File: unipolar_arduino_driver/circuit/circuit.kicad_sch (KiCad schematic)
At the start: 4 parts, among them U1 ULN2803A

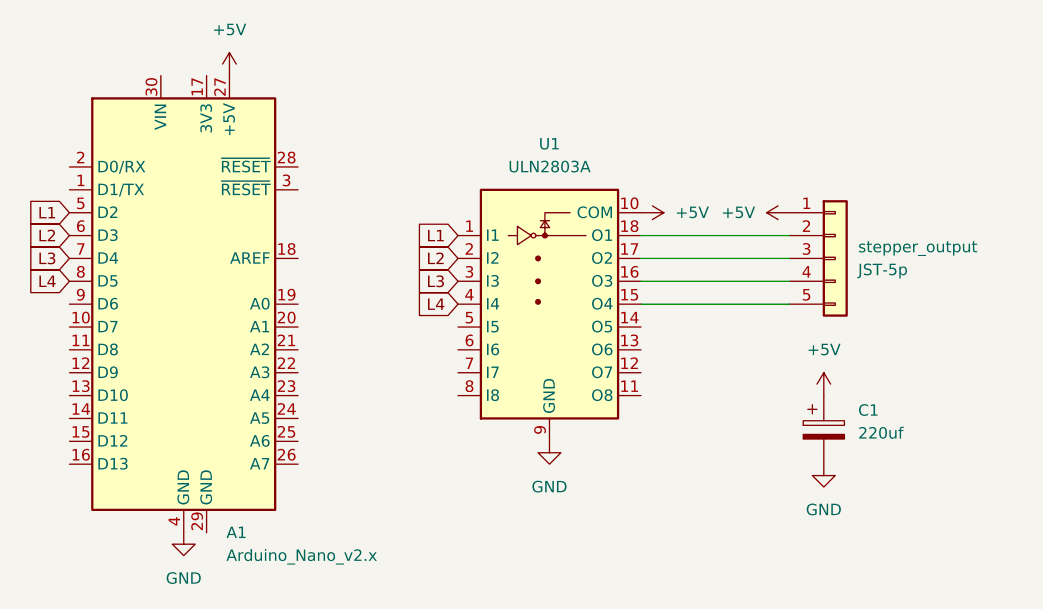
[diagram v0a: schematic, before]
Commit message: finished unipolar driver
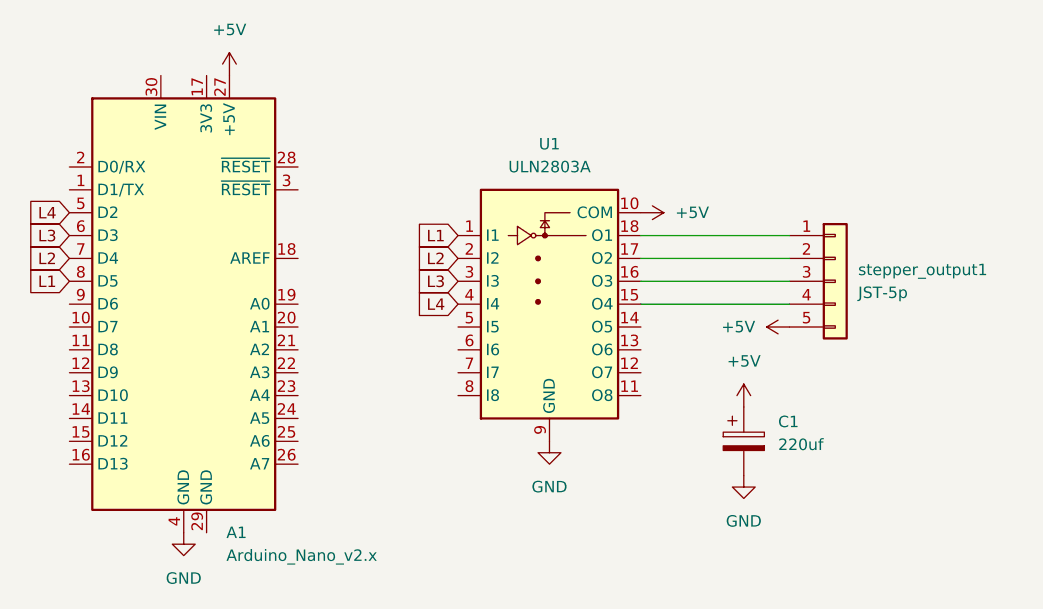
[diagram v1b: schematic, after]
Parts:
- renumbered stepper_output to stepper_output1
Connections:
- net +5V: now also stepper_output1.5 (Pin_5); no longer stepper_output1.1 (Pin_1)
- net L1: now also A1.8 (D5); no longer A1.5 (D2)
- net L2: now also A1.7 (D4); no longer A1.6 (D3)
- net L3: now also A1.6 (D3); no longer A1.7 (D4)
- net L4: now also A1.5 (D2); no longer A1.8 (D5)
- net at U1.18 (O1): now also stepper_output1.1 (Pin_1); no longer stepper_output1.2 (Pin_2)
- net at U1.17 (O2): now also stepper_output1.2 (Pin_2); no longer stepper_output1.3 (Pin_3)
- net at U1.16 (O3): now also stepper_output1.3 (Pin_3); no longer stepper_output1.4 (Pin_4)
- net at U1.15 (O4): now also stepper_output1.4 (Pin_4); no longer stepper_output1.5 (Pin_5)
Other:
- moved on the sheet: C1, stepper_output1
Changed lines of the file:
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@@
 	(global_label "L4"
 		(shape input)
-		(at 92.71 95.25 180)
+		(at 92.71 87.63 180)
 		(fields_autoplaced yes)
 		(effects
@@
 		)
 		(property "Intersheetrefs" "${INTERSHEET_REFS}"
-			(at 87.4872 95.25 0)
+			(at 87.4872 87.63 0)
 			(effects
 				(font
@@
 	(global_label "L3"
 		(shape input)
-		(at 92.71 92.71 180)
+		(at 92.71 90.17 180)
 		(fields_autoplaced yes)
 		(effects
@@
 		)
 		(property "Intersheetrefs" "${INTERSHEET_REFS}"
-			(at 87.4872 92.71 0)
+			(at 87.4872 90.17 0)
 			(effects
 				(font
@@
 	(global_label "L2"
 		(shape input)
-		(at 92.71 90.17 180)
+		(at 92.71 92.71 180)
 		(fields_autoplaced yes)
 		(effects
@@
 		)
 		(property "Intersheetrefs" "${INTERSHEET_REFS}"
-			(at 87.4872 90.17 0)
+			(at 87.4872 92.71 0)
 			(effects
 				(font
@@
 	(global_label "L1"
 		(shape input)
-		(at 92.71 87.63 180)
+		(at 92.71 95.25 180)
 		(fields_autoplaced yes)
 		(effects
@@
 		)
 		(property "Intersheetrefs" "${INTERSHEET_REFS}"
-			(at 87.4872 87.63 0)
+			(at 87.4872 95.25 0)
 			(effects
 				(font
@@
 	(symbol
 		(lib_id "Connector_Generic:Conn_01x05")
-		(at 177.8 92.71 0)
-		(unit 1)
-		(exclude_from_sim no)
-		(in_bom yes)
-		(on_board yes)
-		(dnp no)
-		(fields_autoplaced yes)
-		(property "Reference" "stepper_output"
-			(at 180.34 91.4399 0)
+		(at 177.8 95.25 0)
+		(unit 1)
+		(exclude_from_sim no)
+		(in_bom yes)
+		(on_board yes)
+		(dnp no)
+		(fields_autoplaced yes)
+		(property "Reference" "stepper_output1"
+			(at 180.34 93.9799 0)
 			(effects
 				(font
@@
 		)
 		(property "Value" "JST-5p"
-			(at 180.34 93.9799 0)
+			(at 180.34 96.5199 0)
 			(effects
 				(font
@@
 		)
 		(property "Footprint" "Connector_JST:JST_EH_B5B-EH-A_1x05_P2.50mm_Vertical"
-			(at 177.8 92.71 0)
+			(at 177.8 95.25 0)
 			(effects
 				(font
@@
 		)
 		(property "Datasheet" "~"
-			(at 177.8 92.71 0)
+			(at 177.8 95.25 0)
 			(effects
 				(font
@@
 		)
 		(property "Description" "Generic connector, single row, 01x05, script generated (kicad-library-utils/schlib/autogen/connector/)"
-			(at 177.8 92.71 0)
+			(at 177.8 95.25 0)
 			(effects
 				(font
@@
 			(project ""
 				(path "/d0bfccd7-cc06-4c1b-8a8c-9fcd948798c3"
-					(reference "stepper_output")
+					(reference "stepper_output1")
 					(unit 1)
 				)
@@
 	(symbol
 		(lib_id "power:+5V")
-		(at 172.72 87.63 90)
+		(at 172.72 100.33 90)
 		(unit 1)
 		(exclude_from_sim no)
@@
 		(fields_autoplaced yes)
 		(property "Reference" "#PWR04"
-			(at 176.53 87.63 0)
+			(at 176.53 100.33 0)
 			(effects
 				(font
@@
 		)
 		(property "Value" "+5V"
-			(at 168.91 87.6299 90)
+			(at 168.91 100.3299 90)
 			(effects
 				(font
@@
 		)
 		(property "Footprint" ""
-			(at 172.72 87.63 0)
+			(at 172.72 100.33 0)
 			(effects
 				(font
@@
 		)
 		(property "Datasheet" ""
-			(at 172.72 87.63 0)
+			(at 172.72 100.33 0)
 			(effects
 				(font
@@
 		)
 		(property "Description" "Power symbol creates a global label with name \"+5V\""
-			(at 172.72 87.63 0)
+			(at 172.72 100.33 0)
 			(effects
 				(font
@@
 	(symbol
 		(lib_id "power:GND")
-		(at 176.53 115.57 0)
+		(at 167.64 116.84 0)
 		(unit 1)
 		(exclude_from_sim no)
@@
 		(fields_autoplaced yes)
 		(property "Reference" "#PWR07"
-			(at 176.53 121.92 0)
+			(at 167.64 123.19 0)
 			(effects
 				(font
@@
 		)
 		(property "Value" "GND"
-			(at 176.53 120.65 0)
+			(at 167.64 121.92 0)
 			(effects
 				(font
@@
 		)
 		(property "Footprint" ""
-			(at 176.53 115.57 0)
+			(at 167.64 116.84 0)
 			(effects
 				(font
@@
 		)
 		(property "Datasheet" ""
-			(at 176.53 115.57 0)
+			(at 167.64 116.84 0)
 			(effects
 				(font
@@
 		)
 		(property "Description" "Power symbol creates a global label with name \"GND\" , ground"
-			(at 176.53 115.57 0)
+			(at 167.64 116.84 0)
 			(effects
 				(font
@@
 	(symbol
 		(lib_id "Device:C_Polarized")
-		(at 176.53 111.76 0)
+		(at 167.64 113.03 0)
 		(unit 1)
 		(exclude_from_sim no)
@@
 		(fields_autoplaced yes)
 		(property "Reference" "C1"
-			(at 180.34 109.6009 0)
+			(at 171.45 110.8709 0)
 			(effects
 				(font
@@
 		)
 		(property "Value" "220uf"
-			(at 180.34 112.1409 0)
+			(at 171.45 113.4109 0)
 			(effects
 				(font
@@
 		)
 		(property "Footprint" "Capacitor_THT:CP_Radial_D6.3mm_P2.50mm"
-			(at 177.4952 115.57 0)
+			(at 168.6052 116.84 0)
 			(effects
 				(font
@@
 		)
 		(property "Datasheet" "~"
-			(at 176.53 111.76 0)
+			(at 167.64 113.03 0)
 			(effects
 				(font
@@
 		)
 		(property "Description" "Polarized capacitor"
-			(at 176.53 111.76 0)
+			(at 167.64 113.03 0)
 			(effects
 				(font
@@
 	(symbol
 		(lib_id "power:+5V")
-		(at 176.53 107.95 0)
+		(at 167.64 109.22 0)
 		(unit 1)
 		(exclude_from_sim no)
@@
 		(fields_autoplaced yes)
 		(property "Reference" "#PWR06"
-			(at 176.53 111.76 0)
+			(at 167.64 113.03 0)
 			(effects
 				(font
@@
 		)
 		(property "Value" "+5V"
-			(at 176.53 102.87 0)
+			(at 167.64 104.14 0)
 			(effects
 				(font
@@
 		)
 		(property "Footprint" ""
-			(at 176.53 107.95 0)
+			(at 167.64 109.22 0)
 			(effects
 				(font
@@
 		)
 		(property "Datasheet" ""
-			(at 176.53 107.95 0)
+			(at 167.64 109.22 0)
 			(effects
 				(font
@@
 		)
 		(property "Description" "Power symbol creates a global label with name \"+5V\""
-			(at 176.53 107.95 0)
-			(effects
-				(font
+			(at 167.64 109.22 0)
+			(effects
+				(font
